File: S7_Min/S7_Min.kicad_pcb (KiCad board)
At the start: 4 copper layers, 124 parts, among them J1 Barrel_Jack_Switch, J2 XILINX_JTAG, Q1 DMN2020L, Q2 DMN63D8LDW, Q3 DMN63D8LDW, Q4 DMN63D8LDW, U1 TPS65581, U2 XC7S50-FTGB196, U3 REF3012, U4 QSPI_Flash_SOIC8, U5 MT47H128M16XX, X1 DSC61XX

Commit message: more DDR2 WIP
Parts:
- C56, C58, C59, C60, C61: moved to B.Cu
- moved C56 79.7 mm to (134.0, 99.0), turned to 180 degrees
- moved C59 76.9 mm to (134.0, 98.1), turned to 180 degrees
- moved C58 76.1 mm to (134.6, 101.2)
- moved C61 73.4 mm to (135.0, 94.9)
- moved C60 68.8 mm to (135.0, 94.1)
- moved C50 0.79 mm to (121.5, 97.0)
- moved C57 0.79 mm to (120.5, 97.0)
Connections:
- U2 pad H1: /Bank34/DDR2_A5 -> /Bank34/DDR2_CAS
- U2 pad H2: /Bank34/DDR2_A4 -> /Bank34/DDR2_RAS
- U2 pad H3: /Bank34/DDR2_A3 -> /Bank34/DDR2_ODT
- U2 pad H4: /Bank34/DDR2_A2 -> /Bank34/DDR2_CKE
- U2 pad J1: /Bank34/DDR2_A7 -> /Bank34/DDR2_A2
- U2 pad J2: /Bank34/DDR2_A6 -> /Bank34/DDR2_A0
- U2 pad J3: /Bank34/DDR2_A11 -> /Bank34/DDR2_A4
- U2 pad J4: /Bank34/DDR2_A10 -> /Bank34/DDR2_BA2
- U2 pad K3: /Bank34/DDR2_A9 -> /Bank34/DDR2_A6
- U2 pad K4: /Bank34/DDR2_A8 -> /Bank34/DDR2_BA0
- U2 pad L1: /Bank34/DDR2_A13 -> /Bank34/DDR2_A8
- U2 pad L2: /Bank34/DDR2_BA0 -> /Bank34/DDR2_A13
- U2 pad L3: /Bank34/DDR2_RAS -> /Bank34/DDR2_A11
- U2 pad M1: /Bank34/DDR2_A12 -> /Bank34/DDR2_WE
- U2 pad M2: /Bank34/DDR2_CKE -> /Bank34/DDR2_BA1
- U2 pad M3: /Bank34/DDR2_ODT -> /Bank34/DDR2_A1
- U2 pad M4: /Bank34/DDR2_BA2 -> /Bank34/DDR2_A10
- U2 pad M5: /Bank34/DDR2_BA1 -> /Bank34/DDR2_A7
- U2 pad N1: /Bank34/DDR2_CAS -> /Bank34/DDR2_A5
- U2 pad N4: /Bank34/DDR2_A1 -> /Bank34/DDR2_A3
- U2 pad P2: /Bank34/DDR2_WE -> /Bank34/DDR2_A9
- U2 pad P5: /Bank34/DDR2_A0 -> /Bank34/DDR2_A12
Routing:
- net /Bank34/DDR2_CK+: track 0.57 -> 39.7 mm, vias 1 -> 2
- net /Bank34/DDR2_CK-: track 0.57 -> 39.4 mm, vias 1 -> 2
- net /Bank34/DDR2_A3: track 0.57 -> 36.1 mm, vias 1 -> 2
- net /Bank34/DDR2_A7: track 0.57 -> 30.2 mm, vias 1 -> 2
- net /Bank34/DDR2_A10: track 0.57 -> 29.4 mm, vias 1 -> 2
- net /Bank34/DDR2_BA2: track 0.57 -> 29.1 mm, vias 1 -> 2
- net /Bank34/DDR2_CKE: track 0.57 -> 28.9 mm, vias 1 -> 2
- net /Bank34/DDR2_A12: track 0.57 -> 28.5 mm, vias 1 -> 2
- net /Bank34/DDR2_BA0: track 0.57 -> 28.2 mm, vias 1 -> 2
- net /Bank34/DDR2_A1: track 0.57 -> 25.3 mm, vias 1 -> 0
- net /Bank34/DDR2_BA1: track 0.57 -> 24.3 mm, vias 1 -> 0
- net /Bank34/DDR2_A9: track 0.57 -> 24.3 mm, vias 1 -> 0
- net /Bank34/DDR2_WE: track 0.57 -> 23.7 mm, vias 1 -> 0
- net /Bank34/DDR2_A5: track 3.47 -> 23.0 mm, vias 1 -> 0
- net /Bank34/DDR2_A6: track 9.19 -> 20.1 mm
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
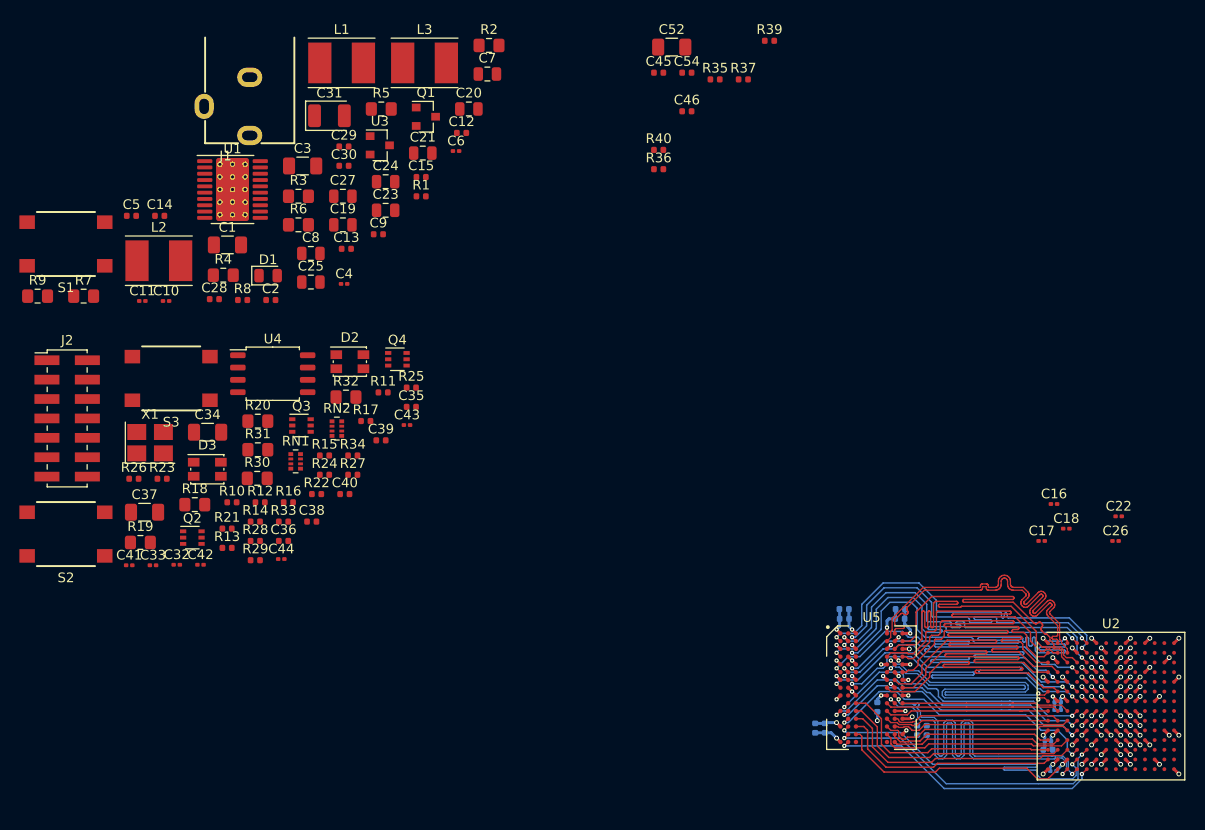
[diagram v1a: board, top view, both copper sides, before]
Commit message: DDR2 interface mostly completed
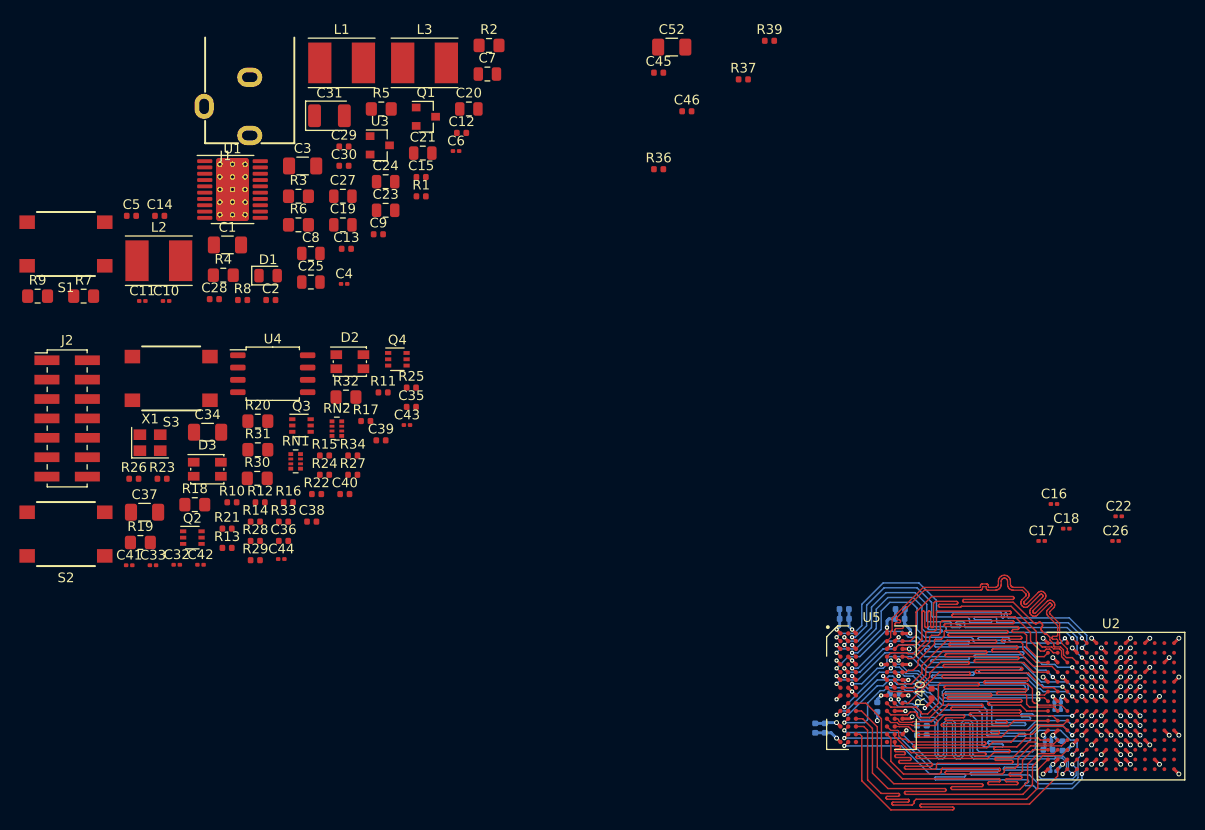
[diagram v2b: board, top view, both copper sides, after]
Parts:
- C54, R35: moved to B.Cu
- X1: footprint Oscillator:Oscillator_SMD_Abracon_ASE-4Pin_3.2x2.5mm_HandSoldering -> Oscillator:Oscillator_SMD_Abracon_ASE-4Pin_3.2x2.5mm
- moved C54 79.5 mm to (135.5, 98.6), turned to 270 degrees
- moved R35 66.0 mm to (118.2, 93.2)
- moved R40 62.7 mm to (122.0, 93.2), turned to 90 degrees
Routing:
- net /Bank34/DDR2_A8: track 16.9 -> 36.0 mm
- net /Bank34/DDR2_CAS: track 17.1 -> 36.1 mm
- net /Bank34/DDR2_A2: track 17.3 -> 36.0 mm
- net /Bank34/DDR2_ODT: track 17.4 -> 36.0 mm
- net /Bank34/DDR2_A0: track 17.5 -> 36.0 mm
- net /Bank34/DDR2_A13: track 17.5 -> 36.0 mm
- net /Bank34/DDR2_RAS: track 18.0 -> 35.9 mm
- net /Bank34/DDR2_A4: track 18.5 -> 36.1 mm
- net /Bank34/DDR2_DQ11: track 52.2 -> 36.1 mm
- net /Bank34/DDR2_A11: track 20.0 -> 35.9 mm
- net /Bank34/DDR2_A6: track 20.1 -> 36.0 mm
- net /Bank34/DDR2_A1: track 25.3 -> 39.6 mm
- net /Bank34/DDR2_A5: track 23.0 -> 36.0 mm
- net /Bank34/DDR2_WE: track 23.7 -> 36.0 mm
- net /Bank34/DDR2_BA1: track 24.3 -> 36.1 mm
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
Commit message: updated board to user custom footprint for 0201 caps
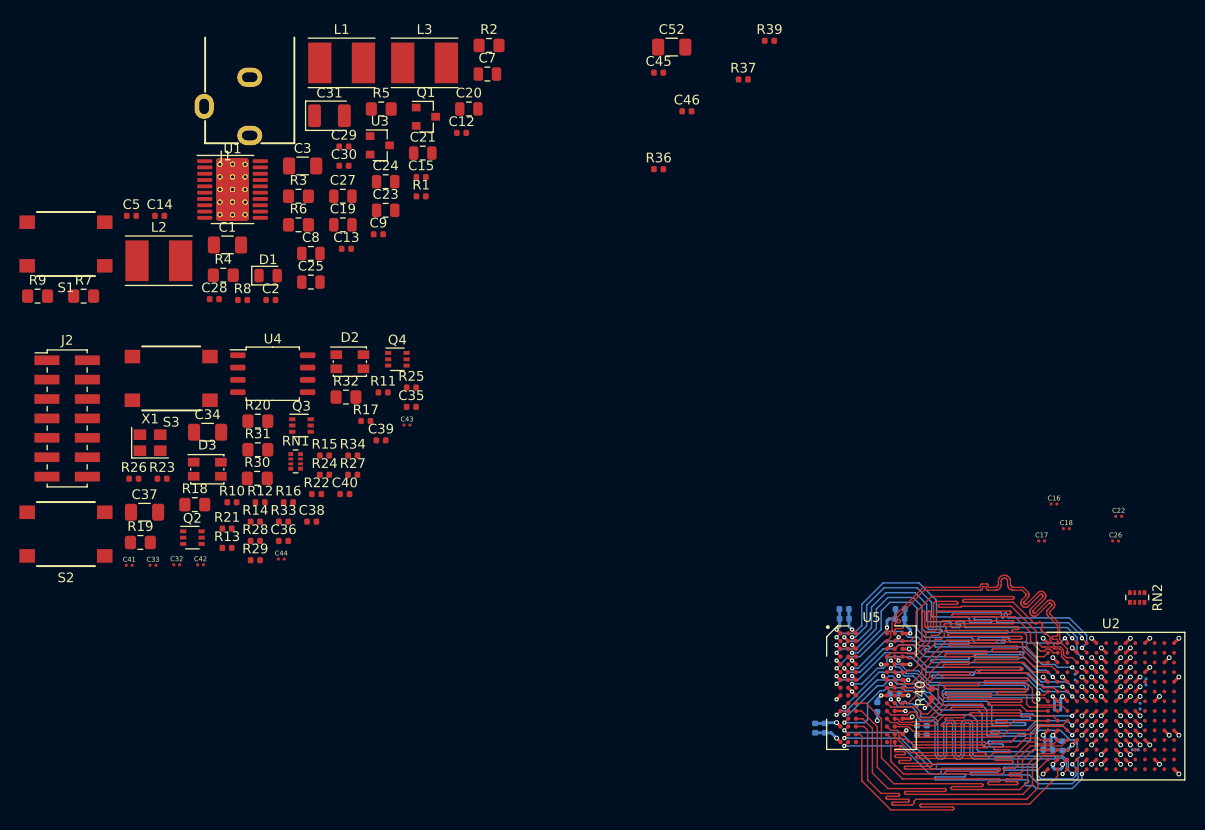
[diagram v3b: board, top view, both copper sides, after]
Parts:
- C10, C11, C4, C6: footprint Capacitor_SMD:C_0201_0603Metric -> my_parts:C_0201_0603Metric; moved to B.Cu
- C16, C17, C18, C22, C26, C32, C33, C41, C42, C43, C44, C58, C59, C60, C61: footprint Capacitor_SMD:C_0201_0603Metric -> my_parts:C_0201_0603Metric
- moved C10 108.4 mm to (144.1, 92.0), turned to 90 degrees
- moved C11 103.7 mm to (136.8, 91.5), turned to 270 degrees
- moved C4 94.7 mm to (143.0, 99.0)
- moved C6 90.8 mm to (143.5, 94.5), turned to 90 degrees
- moved RN2 84.3 mm to (143.2, 83.3), turned to 270 degrees
- moved C58 0.49 mm to (135.0, 101.0)
